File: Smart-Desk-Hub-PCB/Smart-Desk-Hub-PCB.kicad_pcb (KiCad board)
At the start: 2 copper layers, 127 x 106 mm, 5 parts, among them J1 Conn_01x08, J2 Conn_01x07, J3 Conn_01x06, J4 Conn_01x07, U1 ESP32-S3-DevKitC

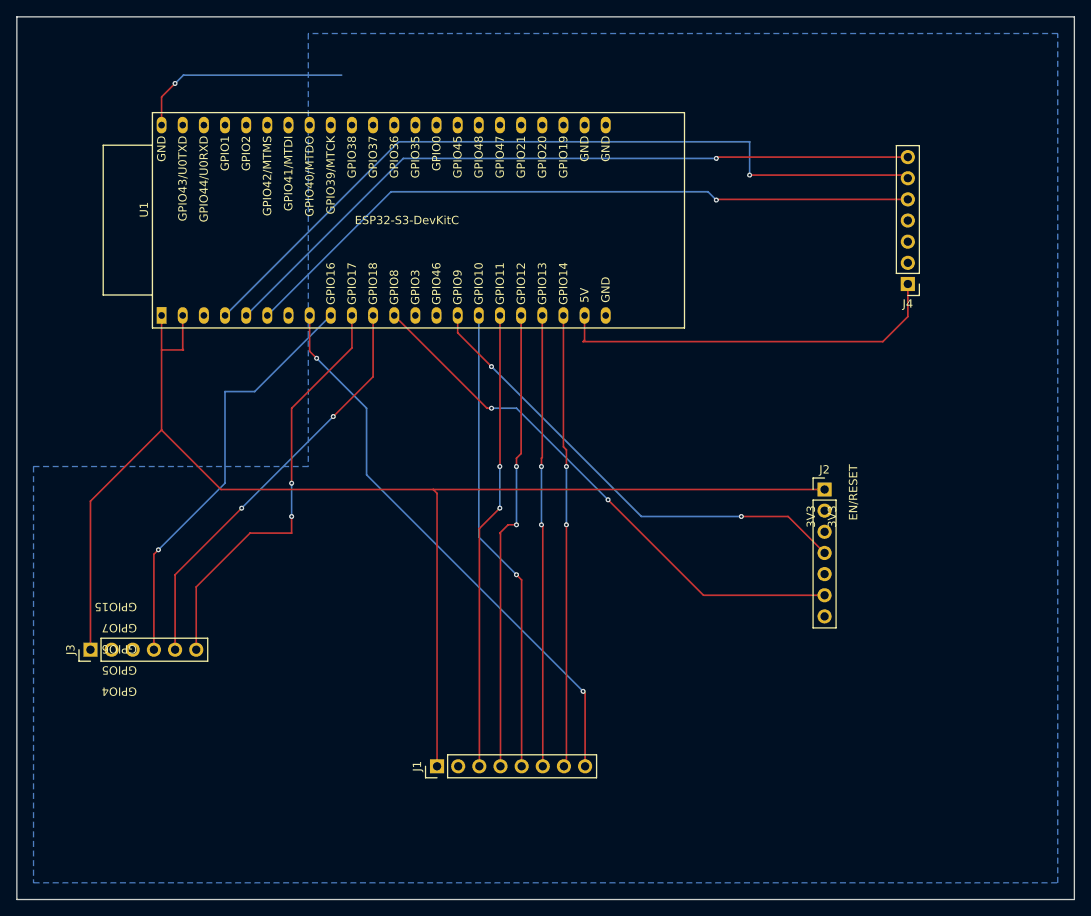
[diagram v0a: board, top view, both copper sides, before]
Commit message: Fix PCB dimensions, add decoupling capacitors, and update Components list and README
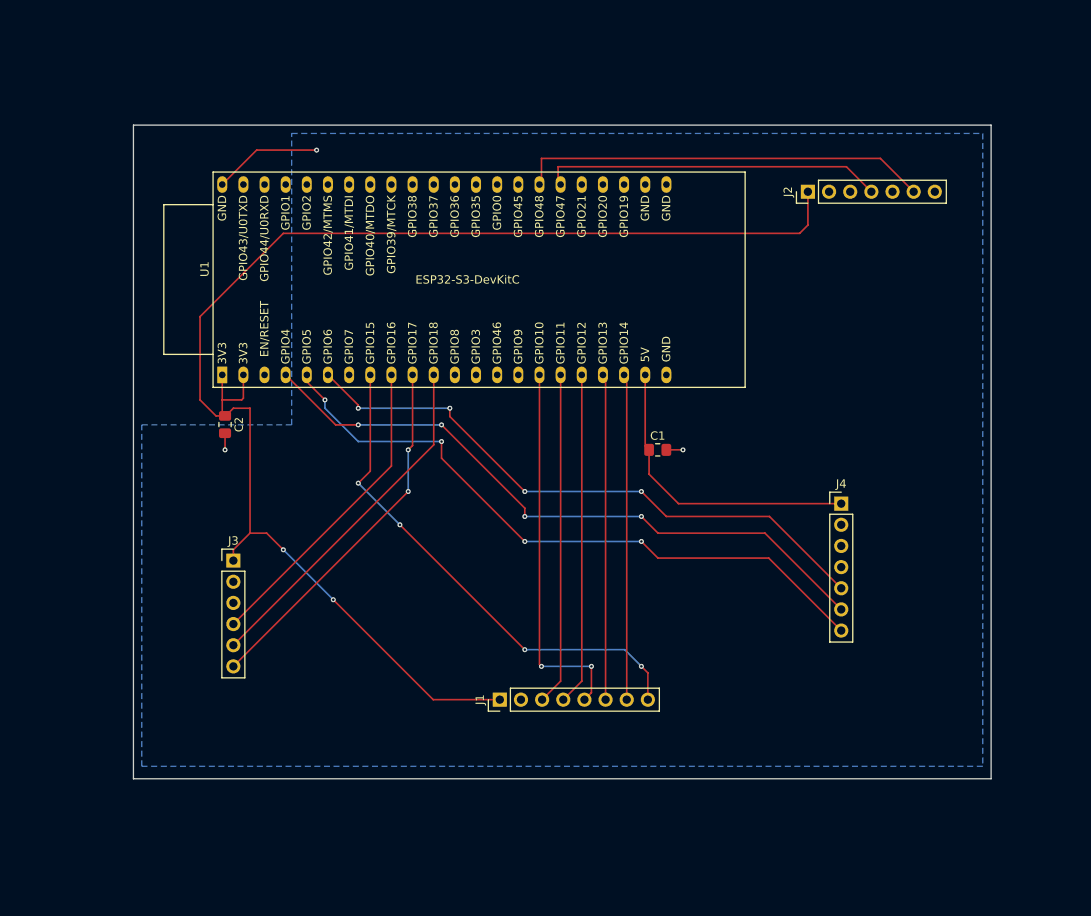
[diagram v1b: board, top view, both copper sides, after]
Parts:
- added C1: 10 µF, Capacitor_SMD:C_0805_2012Metric_Pad1.18x1.45mm_HandSolder, F.Cu at (160.0, 99.0)
- added C2: 10 µF, Capacitor_SMD:C_0805_2012Metric_Pad1.18x1.45mm_HandSolder, F.Cu at (108.0, 96.0)
- moved J2 35.8 mm to (178.0, 68.0), turned to 90 degrees
- moved J4 27.6 mm to (182.0, 105.5), turned to 0 degrees
- moved J3 20.2 mm to (109.0, 112.3), turned to 0 degrees
- moved J1 11.0 mm to (141.0, 129.0)
- moved U1 10.2 mm to (107.7, 90.0)
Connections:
- U1 pad 12: /SDI -> unconnected-(U1-GPIO8/ADC1_CH7-Pad12)
- U1 pad 15: /SCK_TEMP -> unconnected-(U1-GPIO9/ADC1_CH8-Pad15)
- U1 pad 28: unconnected-(U1-GPIO47-Pad28) -> /SCK_TEMP
- U1 pad 29: unconnected-(U1-GPIO48-Pad29) -> /SDI
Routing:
- net /SDI: track 65.6 -> 49.6 mm, vias 2 -> 0
- net /SCK_TEMP: track 57.1 -> 41.1 mm, vias 2 -> 0
- net /CLK: track 55.8 -> 39.9 mm, vias 2 -> 0
- net /BCLK: track 94.8 -> 79.0 mm, vias 1 -> 4
- net /RST: track 54.4 -> 39.1 mm, vias 2 -> 0
- net /DIN: track 55.2 -> 39.9 mm, vias 2 -> 0
- net /DC: track 54.2 -> 39.1 mm, vias 2 -> 0
- net /SCK: track 51.0 -> 37.8 mm, vias 1 -> 0
- net /CS: track 56.3 -> 45.4 mm, vias 1 -> 2
- net +5V: track 47.4 -> 36.7 mm
- net /DIN_SPEAKER: track 83.5 -> 73.1 mm, vias 1 -> 4
- net GND: track 26.1 -> 17.1 mm, vias 1 -> 3
- net /LRC: track 87.3 -> 79.1 mm, vias 1 -> 4
- net /SD: track 50.0 -> 42.4 mm, vias 2 -> 0
- net /WS: track 50.8 -> 43.9 mm
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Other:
- board size 127 x 106 mm -> 103 x 78.5 mm
